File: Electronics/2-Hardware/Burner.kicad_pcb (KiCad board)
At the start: 2 copper layers, 39.4 x 22.9 mm, 16 parts, among them P1 CONN_2, P2 CONN_2, P3 CONN_1, P4 CONN_2, P5 CONN_2, P6 CONN_1, Q1 MOSFET_N, U1 LM317-4PIN, U2 MSP430G2553-20, U3 DIFF_RX

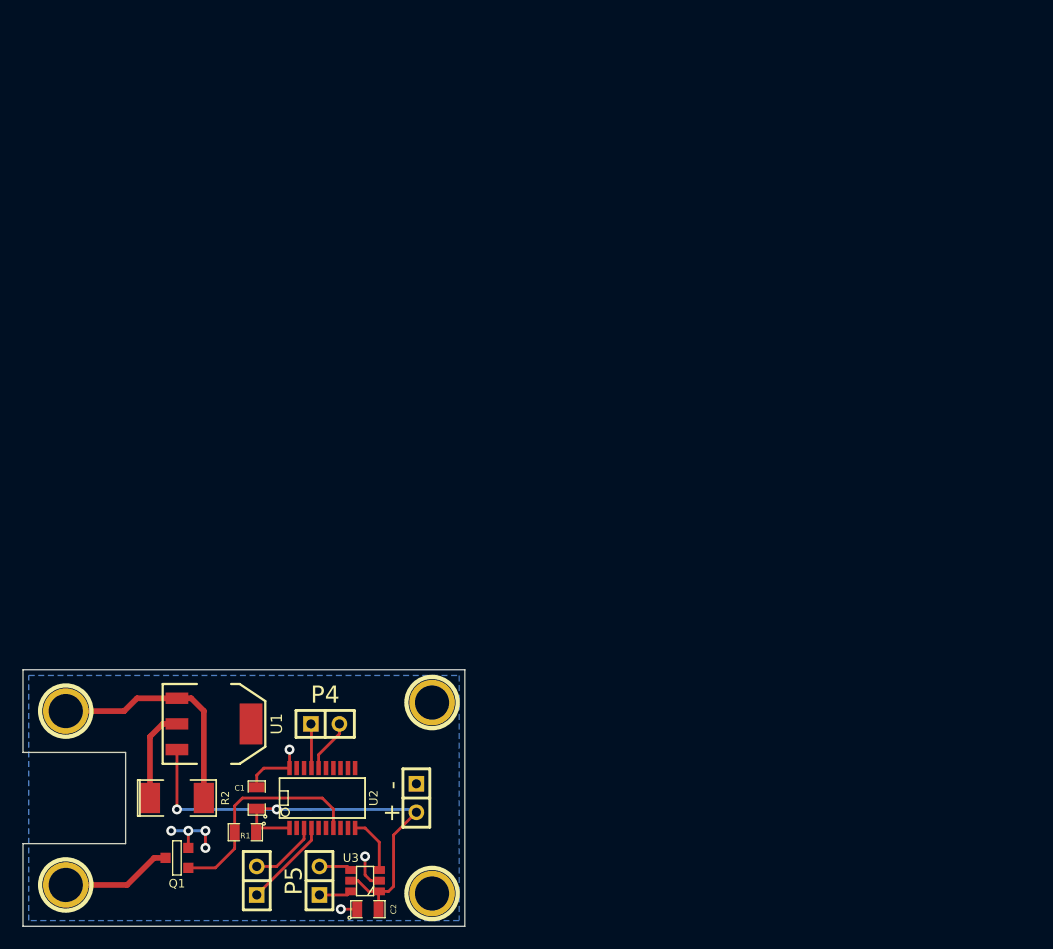
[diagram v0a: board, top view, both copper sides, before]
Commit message: F23 update to burner
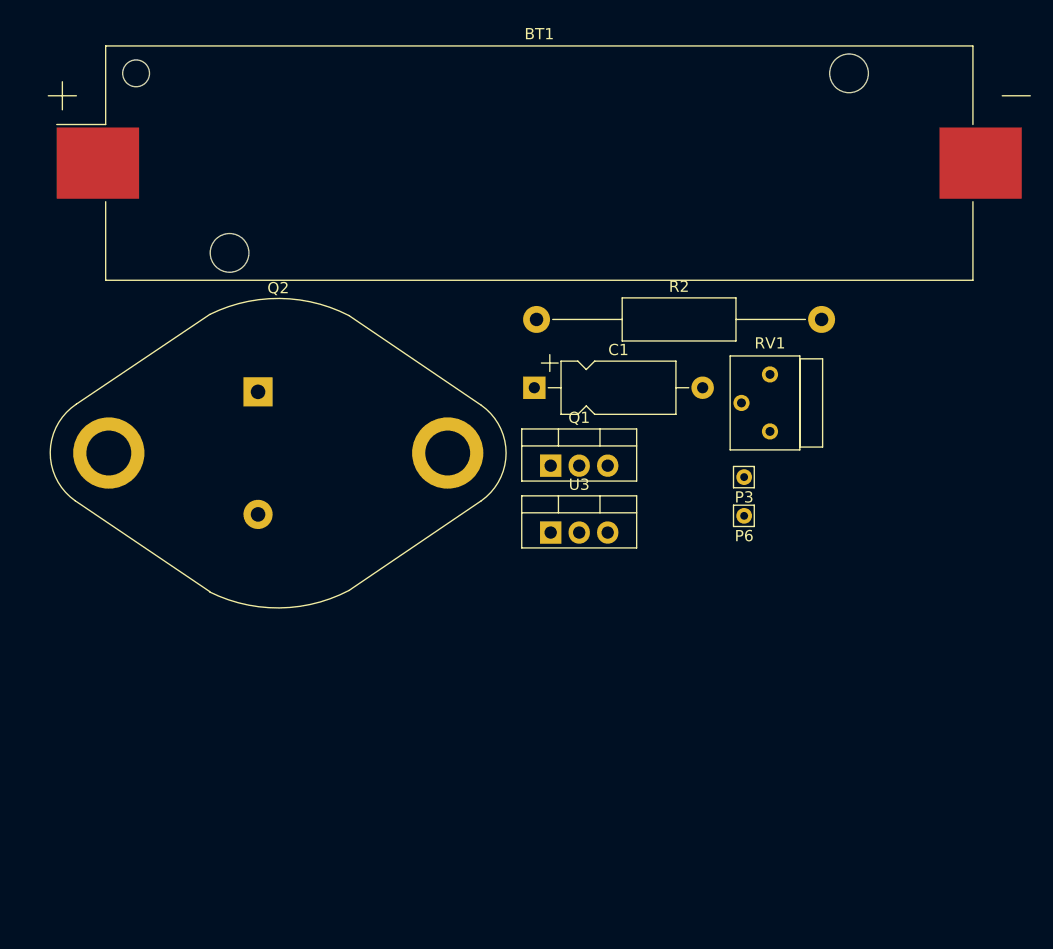
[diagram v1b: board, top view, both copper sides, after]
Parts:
- removed 1PIN (x2): P***, 1pin
- removed C2: 0.1uF, SM0805
- removed P1, P2, P4, P5: CONN_2, CONN_1x2
- removed R1: 10k, SM0805
- removed U1: LM317-4PIN, SOT223
- removed U2: MSP430G2553-20, SSOP20
- added BT1: Battery, Battery:BatteryHolder_Keystone_1042_1x18650, F.Cu at (197.6, 113.3)
- added Q2: MJ2955, Package_TO_SOT_THT:TO-3, F.Cu at (172.6, 133.7)
- added RV1: 0-1k, Potentiometer_THT:Potentiometer_Bourns_3339S_Horizontal, F.Cu at (218.2, 132.2)
- C1: value 1uF -> 10 uF; footprint SM0805 -> Capacitor_THT:CP_Axial_L10.0mm_D4.5mm_P15.00mm_Horizontal
- P3, P6: footprint 1pin -> Connector_Pin:Pin_D0.7mm_L6.5mm_W1.8mm_FlatFork
- Q1: value MOSFET_N -> TIP120; footprint SOT23GDS -> Package_TO_SOT_THT:TO-220-3_Vertical
- R2: value 2.7 -> 10; footprint SM2010 -> Resistor_THT:R_Axial_DIN0411_L9.9mm_D3.6mm_P25.40mm_Horizontal
- U3: value DIFF_RX -> LM317_TO-220; footprint SOT23_6 -> Package_TO_SOT_THT:TO-220-3_Vertical
- moved P6 68.8 mm to (215.9, 144.8)
- moved P3 63.9 mm to (215.9, 141.3)
- moved R2 53.3 mm to (197.4, 127.3)
- moved Q1 48.3 mm to (198.7, 140.3), turned to 0 degrees
- moved C1 44.1 mm to (197.2, 133.4), turned to 0 degrees
- moved U3 35.2 mm to (198.7, 146.3), turned to 0 degrees
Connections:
- C1 pad 1: +BATT -> Net-(Q2-B)
- C1 pad 2: GND -> Net-(Q1-C)
- P3 pad 1: /Ni_+ -> B_OUT
- P6 pad 1: /NI_- -> GND
- R2 pad 1: /NI_Out -> Net-(U3-VO)
- R2 pad 2: /Ni_+ -> Net-(R2-Pad2)
- U3 pad 1: +BATT -> unconnected-(U3-ADJ-Pad1)
- U3 pad 2: GND -> Net-(U3-VO)
- U3 pad 3: /DATA_IN -> Net-(Q2-B)
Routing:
- net +BATT: track 47.2 -> 0.00 mm, vias 2 -> 0
- net /Ni_+: track 21.0 -> 0.00 mm
- net /MOS_TRIG: track 19.8 -> 0.00 mm
- net GND: track 16.6 -> 0.00 mm, vias 7 -> 0
- net /NI_-: track 9.89 -> 0.00 mm
- net /NI_Out: track 8.34 -> 0.00 mm
- net N-000006: track 7.99 -> 0.00 mm
- net N-000005: track 6.22 -> 0.00 mm
- net /DATA_IN: track 5.16 -> 0.00 mm
- net N-000001: track 4.71 -> 0.00 mm
- net N-000007: track 3.96 -> 0.00 mm
- net N-000002: track 2.93 -> 0.00 mm
- net N-000003: track 2.93 -> 0.00 mm
- removed copper zone on B.Cu, net GND
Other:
- board outline removed
- net class Default removed
- net class NichromePower removed
- board text removed: "+"
- board text removed: "-"
